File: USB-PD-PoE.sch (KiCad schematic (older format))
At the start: 126 parts, among them J1 8P8C_Shielded, J2 8P8C_Shielded, J3 TagConnect_TC2030_SWD, J4 USB_C_Receptacle_USB2.0, Q1 FDC2512, Q2 2N7002, Q3 2N7002, Q4 2N7002, Q5 APM4953KC, T1 HR051142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

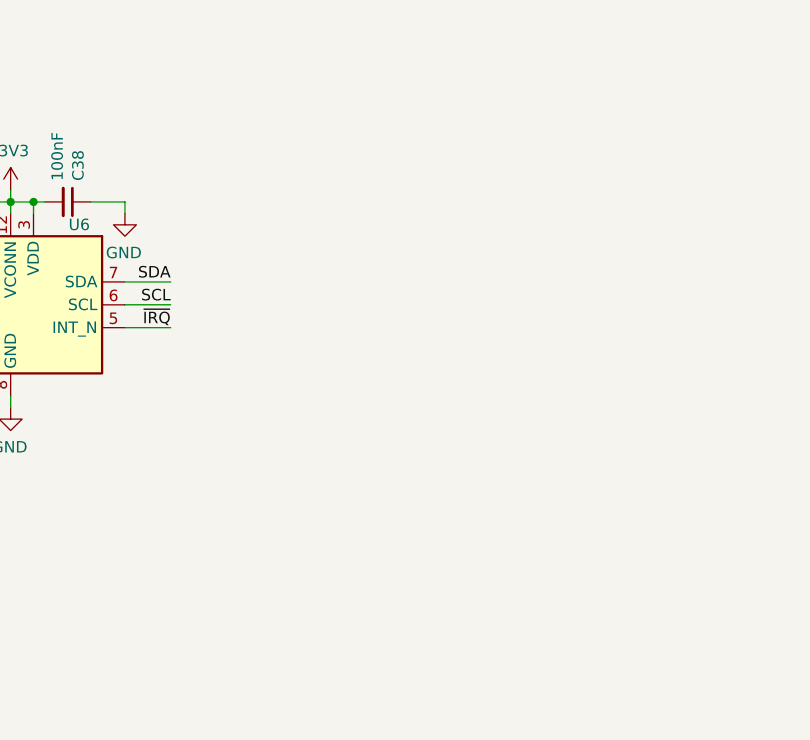
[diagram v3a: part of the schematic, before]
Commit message: Add USB/CC protection diode
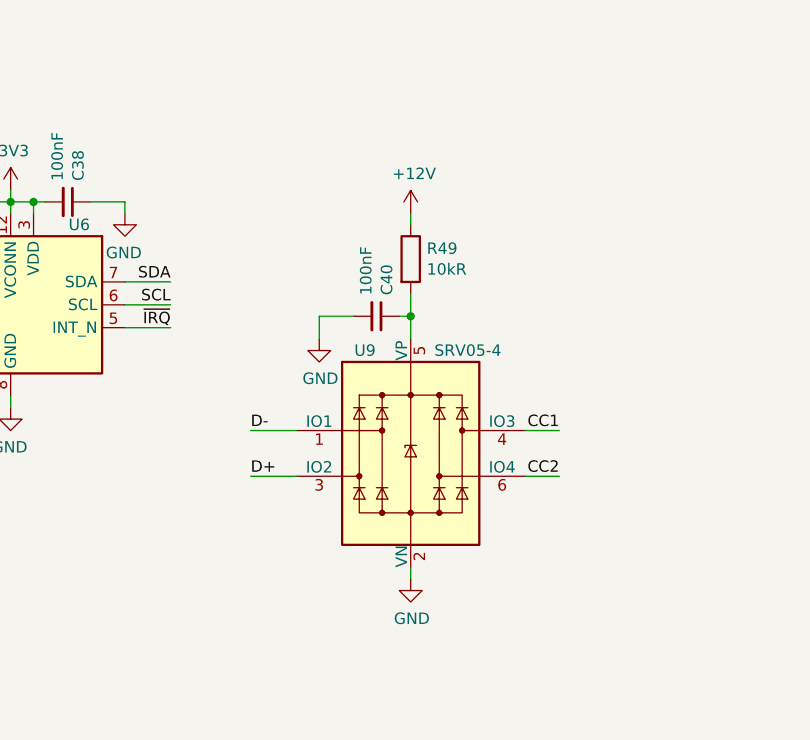
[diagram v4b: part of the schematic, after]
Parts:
- added C40: 100nF, Capacitor_SMD:C_0402_1005Metric, symbol Device:C_Small
- added R49: 10kR, Resistor_SMD:R_0402_1005Metric, symbol Device:R
- added U9: SRV05-4, Package_TO_SOT_SMD:SOT-23-6, symbol Power_Protection:SRV05-4
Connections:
- net +12V: now also R49.1
- net CC1: now also U9.4 (IO3)
- net CC2: now also U9.6 (IO4)
- net D+: now also U9.3 (IO2)
- net D-: now also U9.1 (IO1)
- net GND: now also C40.2, U9.2 (VN)
- new net: C40.1, R49.2, U9.5 (VP)
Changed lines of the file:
@@
 	1    0    0    -1
 $EndComp
+$Comp
+L Power_Protection:SRV05-4 U9
+U 1 1 64F616A2
+P 7800 9700
+F 0 "U9" H 7600 10150 50  0000 C CNN
+F 1 "SRV05-4" H 8050 10150 50  0000 C CNN
+F 2 "Package_TO_SOT_SMD:SOT-23-6" H 8500 9250 50  0001 C CNN
+F 3 "http://www.onsemi.com/pub/Collateral/SRV05-4-D.PDF" H 7800 9700 50  0001 C CNN
+F 4 "C85364" H 7800 9700 50  0001 C CNN "LCSC"
+	1    7800 9700
+	1    0    0    -1
+$EndComp
+$Comp
+L Device:R R49
+U 1 1 64F63DEA
+P 7800 8850
+F 0 "R49" H 7870 8896 50  0000 L CNN
+F 1 "10kR" H 7870 8805 50  0000 L CNN
+F 2 "Resistor_SMD:R_0402_1005Metric" V 7730 8850 50  0001 C CNN
+F 3 "~" H 7800 8850 50  0001 C CNN
+F 4 "C25744" H 7800 8850 50  0001 C CNN "LCSC"
+	1    7800 8850
+	1    0    0    -1
+$EndComp
+$Comp
+L Device:C_Small C40
+U 1 1 64FABF15
+P 7650 9100
+F 0 "C40" H 7742 9146 50  0000 L CNN
+F 1 "100nF" H 7742 9055 50  0000 L CNN
+F 2 "Capacitor_SMD:C_0402_1005Metric" H 7650 9100 50  0001 C CNN
+F 3 "~" H 7650 9100 50  0001 C CNN
+F 4 "C1525" H 7650 9100 50  0001 C CNN "LCSC"
+	1    7650 9100
+	0    1    -1   0
+$EndComp
+Wire Wire Line
+	7800 9200 7800 9100
+Wire Wire Line
+	7750 9100 7800 9100
+Connection ~ 7800 9100
+Wire Wire Line
+	7800 9100 7800 9000
+$Comp
+L power:GND #PWR0137
+U 1 1 65088998
+P 7400 9200
+F 0 "#PWR0137" H 7400 8950 50  0001 C CNN
+F 1 "GND" H 7405 9027 50  0000 C CNN
+F 2 "" H 7400 9200 50  0001 C CNN
+F 3 "" H 7400 9200 50  0001 C CNN
+	1    7400 9200
+	1    0    0    -1
+$EndComp
+Wire Wire Line
+	7400 9200 7400 9100
+Wire Wire Line
+	7400 9100 7550 9100
+$Comp
+L power:+12V #PWR0138
+U 1 1 650D4163
+P 7800 8650
+F 0 "#PWR0138" H 7800 8500 50  0001 C CNN
+F 1 "+12V" H 7815 8823 50  0000 C CNN
+F 2 "" H 7800 8650 50  0001 C CNN
+F 3 "" H 7800 8650 50  0001 C CNN
+	1    7800 8650
+	1    0    0    -1
+$EndComp
+Wire Wire Line
+	7800 8650 7800 8700
+Wire Wire Line
+	7300 9600 7100 9600
+Text Label 7100 9600 0    50   ~ 0
+D-
+Wire Wire Line
+	7300 9800 7100 9800
+Text Label 7100 9800 0    50   ~ 0
+D+
+Wire Wire Line
+	8300 9600 8450 9600
+Text Label 8450 9600 2    50   ~ 0
+CC1
+Wire Wire Line
+	8300 9800 8450 9800
+Text Label 8450 9800 2    50   ~ 0
+CC2
+$Comp
+L power:GND #PWR0139
+U 1 1 652C53BE
+P 7800 10250
+F 0 "#PWR0139" H 7800 10000 50  0001 C CNN
+F 1 "GND" H 7805 10077 50  0000 C CNN
+F 2 "" H 7800 10250 50  0001 C CNN
+F 3 "" H 7800 10250 50  0001 C CNN
+	1    7800 10250
+	1    0    0    -1
+$EndComp
+Wire Wire Line
+	7800 10250 7800 10200
 $EndSCHEMATC

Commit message: Fix reversed CJ431 pinout
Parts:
- U4: symbol Reference_Voltage:TL431DBZ -> Reference_Voltage:CJ432
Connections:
- net at C12.2, D7.2 (A), R17.2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: now also U4.2 (K); no longer U4.1 (K)
- net at C12.1, C13.1, R18.1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: now also U4.1 (REF); no longer U4.2 (REF)
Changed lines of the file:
@@
 	3350 1750 3350 2000
 $Comp
-L Reference_Voltage:TL431DBZ U4
+L Reference_Voltage:CJ432 U4
 U 1 1 60798E19
 P 6850 2400

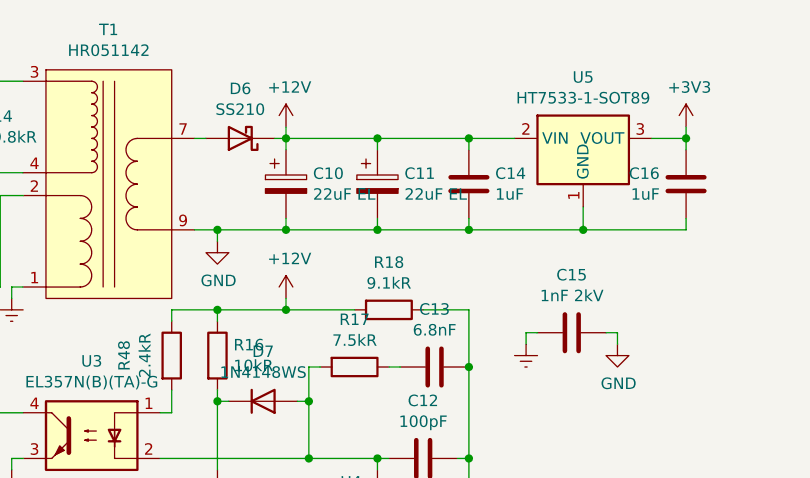
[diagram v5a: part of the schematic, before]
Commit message: Add more bulk capacitance on flyback output
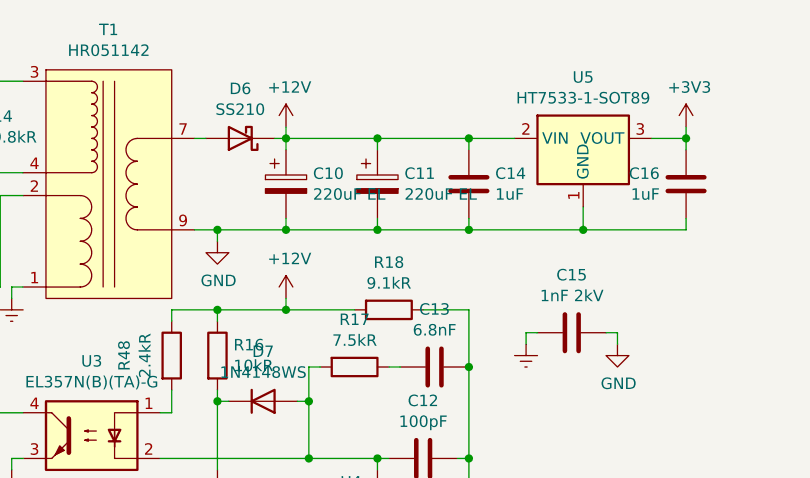
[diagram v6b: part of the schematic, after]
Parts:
- C10, C11: value 22uF EL -> 220uF EL; LCSC C134761 -> C127327
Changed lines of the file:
@@
 P 6450 1050
 F 0 "C10" H 6568 1096 50  0000 L CNN
-F 1 "22uF EL" H 6568 1005 50  0000 L CNN
+F 1 "220uF EL" H 6568 1005 50  0000 L CNN
 F 2 "Capacitor_SMD:CP_Elec_6.3x7.7" H 6488 900 50  0001 C CNN
 F 3 "~" H 6450 1050 50  0001 C CNN
-F 4 "C134761" H 6450 1050 50  0001 C CNN "LCSC"
+F 4 "C127327" H 6450 1050 50  0001 C CNN "LCSC"
 	1    6450 1050
 	1    0    0    -1
@@
 P 6850 1050
 F 0 "C11" H 6968 1096 50  0000 L CNN
-F 1 "22uF EL" H 6968 1005 50  0000 L CNN
+F 1 "220uF EL" H 6968 1005 50  0000 L CNN
 F 2 "Capacitor_SMD:CP_Elec_6.3x7.7" H 6888 900 50  0001 C CNN
 F 3 "~" H 6850 1050 50  0001 C CNN
-F 4 "C134761" H 6850 1050 50  0001 C CNN "LCSC"
+F 4 "C127327" H 6850 1050 50  0001 C CNN "LCSC"
 	1    6850 1050
 	1    0    0    -1

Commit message: Add buck converter power gating
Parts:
- added Q6: 2N7002, Package_TO_SOT_SMD:SOT-23, symbol Transistor_FET:2N7002
- added R50, R51: 100kR, Resistor_SMD:R_0402_1005Metric, symbol Device:R_Small
- added R52: 15kR, Resistor_SMD:R_0402_1005Metric, symbol Device:R_Small
- added R53: 10kR, Resistor_SMD:R_0402_1005Metric, symbol Device:R
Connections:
- net BOOST_OUT: no longer Q5.1 (S)
- net GND: now also Q6.2 (S), R50.1
- net VBUS: now also Q5.1 (S), R51.1; no longer C29.1, C31.1, C39.1, L3.2, Q5.7 (D), Q5.8 (G), R31.1
- net BUCK_OUT_EN: now reaches U1.25 (PC5)
- net BUCK_OUT_EN: now also Q6.1 (G), R50.2
- net at Q5.4 (G), R39.1: now also R53.1; no longer Q4.3 (D), Q5.2 (G)
- new net: Q5.2 (G), R51.2, R52.2
- new net: Q6.3 (D), R52.1
- new net: Q4.3 (D), R53.2
- new net BUCK_OUT: C29.1, C31.1, C39.1, L3.2, Q5.7 (D), Q5.8 (G), R31.1
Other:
- moved on the sheet: Q4, Q5A, R40
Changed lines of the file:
@@
 L Device:Q_DUAL_PMOS_S1G1S2G2D2D2D1D1 Q5
 U 1 1 62480DAF
-P 16950 2650
-F 0 "Q5" V 17375 2650 50  0000 C CNN
-F 1 "APM4953KC" V 17284 2650 50  0000 C CNN
-F 2 "Package_SO:SO-8_3.9x4.9mm_P1.27mm" H 17000 2650 50  0001 C CNN
-F 3 "~" H 17000 2650 50  0001 C CNN
-F 4 "C20897" H 16950 2650 50  0001 C CNN "LCSC"
-	1    16950 2650
-	0    1    -1   0
+P 17350 4700
+F 0 "Q5" V 17775 4700 50  0000 C CNN
+F 1 "APM4953KC" V 17684 4700 50  0000 C CNN
+F 2 "Package_SO:SO-8_3.9x4.9mm_P1.27mm" H 17400 4700 50  0001 C CNN
+F 3 "~" H 17400 4700 50  0001 C CNN
+F 4 "C20897" H 17350 4700 50  0001 C CNN "LCSC"
+	1    17350 4700
+	0    -1   -1   0
 $EndComp
 $Comp
@@
 Wire Wire Line
 	16750 2550 16650 2550
-Connection ~ 16750 2550
 $Comp
 L Device:R_Small R39
@@
 Wire Wire Line
 	16950 2900 16950 2850
-Connection ~ 16950 2850
 Wire Wire Line
 	16650 2900 16650 2550
 Connection ~ 16650 2550
-Wire Wire Line
-	16950 3050 16950 2900
-Connection ~ 16950 2900
-Text Label 16100 3250 0    50   ~ 0
+Text Label 16100 3500 0    50   ~ 0
 BOOST_OUT_EN
 Wire Wire Line
-	16100 3250 16600 3250
+	16100 3500 16600 3500
 $Comp
 L Transistor_FET:2N7002 Q2
@@
 L Transistor_FET:2N7002 Q4
 U 1 1 62639897
-P 16850 3250
-F 0 "Q4" H 17054 3296 50  0000 L CNN
-F 1 "2N7002" H 17054 3205 50  0000 L CNN
-F 2 "Package_TO_SOT_SMD:SOT-23" H 17050 3175 50  0001 L CIN
-F 3 "https://www.onsemi.com/pub/Collateral/NDS7002A-D.PDF" H 16850 3250 50  0001 L CNN
-F 4 "C8545" H 16850 3250 50  0001 C CNN "LCSC"
-	1    16850 3250
+P 16850 3500
+F 0 "Q4" H 17054 3546 50  0000 L CNN
+F 1 "2N7002" H 17054 3455 50  0000 L CNN
+F 2 "Package_TO_SOT_SMD:SOT-23" H 17050 3425 50  0001 L CIN
+F 3 "https://www.onsemi.com/pub/Collateral/NDS7002A-D.PDF" H 16850 3500 50  0001 L CNN
+F 4 "C8545" H 16850 3500 50  0001 C CNN "LCSC"
+	1    16850 3500
 	1    0    0    -1
 $EndComp
@@
 L Device:R_Small R40
 U 1 1 62666D7F
-P 16800 3500
-F 0 "R40" H 16859 3546 50  0000 L CNN
-F 1 "100kR" H 16859 3455 50  0000 L CNN
-F 2 "Resistor_SMD:R_0402_1005Metric" H 16800 3500 50  0001 C CNN
-F 3 "~" H 16800 3500 50  0001 C CNN
-F 4 "C25741" H 16800 3500 50  0001 C CNN "LCSC"
-	1    16800 3500
+P 16800 3750
+F 0 "R40" H 16859 3796 50  0000 L CNN
+F 1 "100kR" H 16859 3705 50  0000 L CNN
+F 2 "Resistor_SMD:R_0402_1005Metric" H 16800 3750 50  0001 C CNN
+F 3 "~" H 16800 3750 50  0001 C CNN
+F 4 "C25741" H 16800 3750 50  0001 C CNN "LCSC"
+	1    16800 3750
 	0    1    1    0
 $EndComp
 Wire Wire Line
-	16900 3500 16950 3500
-Wire Wire Line
-	16950 3500 16950 3450
-Wire Wire Line
-	16700 3500 16600 3500
-Wire Wire Line
-	16600 3500 16600 3250
-Connection ~ 16600 3250
-Wire Wire Line
-	16600 3250 16650 3250
+	16900 3750 16950 3750
+Wire Wire Line
+	16950 3750 16950 3700
+Wire Wire Line
+	16700 3750 16600 3750
+Wire Wire Line
+	16600 3750 16600 3500
+Connection ~ 16600 3500
+Wire Wire Line
+	16600 3500 16650 3500
 $Comp
 L power:GND #PWR0118
 U 1 1 626E8989
-P 16950 3550
-F 0 "#PWR0118" H 16950 3300 50  0001 C CNN
-F 1 "GND" H 16955 3377 50  0000 C CNN
-F 2 "" H 16950 3550 50  0001 C CNN
-F 3 "" H 16950 3550 50  0001 C CNN
-	1    16950 3550
-	1    0    0    -1
-$EndComp
-Wire Wire Line
-	16950 3550 16950 3500
-Connection ~ 16950 3500
+P 16950 3800
+F 0 "#PWR0118" H 16950 3550 50  0001 C CNN
+F 1 "GND" H 16955 3627 50  0000 C CNN
+F 2 "" H 16950 3800 50  0001 C CNN
+F 3 "" H 16950 3800 50  0001 C CNN
+	1    16950 3800
+	1    0    0    -1
+$EndComp
+Wire Wire Line
+	16950 3800 16950 3750
+Connection ~ 16950 3750
 $Comp
 L power:VBUS #PWR0119
@@
 Wire Wire Line
 	17150 2450 17200 2450
-Connection ~ 17150 2450
 Wire Wire Line
 	17150 2550 17200 2550
 Wire Wire Line
 	17200 2550 17200 2450
-Connection ~ 17150 2550
 Connection ~ 17200 2450
 Wire Wire Line
@@
 Wire Wire Line
 	16400 4650 16400 4600
-Connection ~ 16400 4600
-Wire Wire Line
-	16400 4600 17750 4600
 Wire Wire Line
 	16400 4850 16400 4900
@@
 Wire Wire Line
 	7800 10250 7800 10200
+Wire Wire Line
+	17550 4600 17650 4600
+Wire Wire Line
+	17150 4600 17100 4600
+Connection ~ 16400 4600
+Wire Wire Line
+	17150 4500 17100 4500
+Wire Wire Line
+	17100 4500 17100 4600
+Connection ~ 17100 4600
+Wire Wire Line
+	17100 4600 16400 4600
+$Comp
+L Device:R_Small R51
+U 1 1 60885FEE
+P 17500 4950
+F 0 "R51" H 17559 4996 50  0000 L CNN
+F 1 "100kR" H 17559 4905 50  0000 L CNN
+F 2 "Resistor_SMD:R_0402_1005Metric" H 17500 4950 50  0001 C CNN
+F 3 "~" H 17500 4950 50  0001 C CNN
+F 4 "C25741" H 17500 4950 50  0001 C CNN "LCSC"
+	1    17500 4950
+	0    1    1    0
+$EndComp
+Wire Wire Line
+	17350 4900 17350 4950
+Wire Wire Line
+	17350 4950 17400 4950
+Wire Wire Line
+	17650 4600 17650 4950
+Wire Wire Line
+	17650 4950 17600 4950
+Connection ~ 17650 4600
+Wire Wire Line
+	17650 4600 17750 4600
+Wire Wire Line
+	17050 5600 17050 5800
+Wire Wire Line
+	17250 5800 17350 5800
+Text Label 16500 5600 0    50   ~ 0
+BUCK_OUT_EN
+$Comp
+L power:GND #PWR0140
+U 1 1 6097046C
+P 17350 5850
+F 0 "#PWR0140" H 17350 5600 50  0001 C CNN
+F 1 "GND" H 17355 5677 50  0000 C CNN
+F 2 "" H 17350 5850 50  0001 C CNN
+F 3 "" H 17350 5850 50  0001 C CNN
+	1    17350 5850
+	1    0    0    -1
+$EndComp
+Wire Wire Line
+	17350 5850 17350 5800
+$Comp
+L Device:R_Small R50
+U 1 1 60970474
+P 17150 5800
+F 0 "R50" H 17209 5846 50  0000 L CNN
+F 1 "100kR" H 17209 5755 50  0000 L CNN
+F 2 "Resistor_SMD:R_0402_1005Metric" H 17150 5800 50  0001 C CNN
+F 3 "~" H 17150 5800 50  0001 C CNN
+F 4 "C25741" H 17150 5800 50  0001 C CNN "LCSC"
+	1    17150 5800
+	0    1    1    0
+$EndComp
+$Comp
+L Transistor_FET:2N7002 Q6
+U 1 1 6097047B
+P 17250 5600
+F 0 "Q6" H 17454 5646 50  0000 L CNN
+F 1 "2N7002" H 17454 5555 50  0000 L CNN
+F 2 "Package_TO_SOT_SMD:SOT-23" H 17450 5525 50  0001 L CIN
+F 3 "https://www.onsemi.com/pub/Collateral/NDS7002A-D.PDF" H 17250 5600 50  0001 L CNN
+F 4 "C8545" H 17250 5600 50  0001 C CNN "LCSC"
+	1    17250 5600
+	1    0    0    -1
+$EndComp
+Connection ~ 17350 5800
+Connection ~ 17050 5600
+Wire Wire Line
+	16500 5600 17050 5600
+Text Label -4950 5350 0    50   ~ 0
+BUCK_OUT_EN
+Wire Wire Line
+	-4950 5350 -4400 5350
+$Comp
+L Device:R_Small R52
+U 1 1 60B3D914
+P 17350 5250
+F 0 "R52" H 17409 5296 50  0000 L CNN
+F 1 "15kR" H 17409 5205 50  0000 L CNN
+F 2 "Resistor_SMD:R_0402_1005Metric" H 17350 5250 50  0001 C CNN
+F 3 "~" H 17350 5250 50  0001 C CNN
+F 4 "C25756" H 17350 5250 50  0001 C CNN "LCSC"
+	1    17350 5250
+	-1   0    0    1
+$EndComp
+Wire Wire Line
+	17350 5400 17350 5350
+Wire Wire Line
+	17350 5150 17350 4950
+Connection ~ 17350 4950
+$Comp
+L Device:R R53
+U 1 1 60C301E8
+P 16950 3100
+F 0 "R53" H 17020 3146 50  0000 L CNN
+F 1 "10kR" H 17020 3055 50  0000 L CNN
+F 2 "Resistor_SMD:R_0402_1005Metric" V 16880 3100 50  0001 C CNN
+F 3 "~" H 16950 3100 50  0001 C CNN
+F 4 "C25744" H 16950 3100 50  0001 C CNN "LCSC"
+	1    16950 3100
+	1    0    0    -1
+$EndComp
+Wire Wire Line
+	16950 2950 16950 2900
+Connection ~ 16950 2900
+Wire Wire Line
+	16950 3250 16950 3300
 $EndSCHEMATC

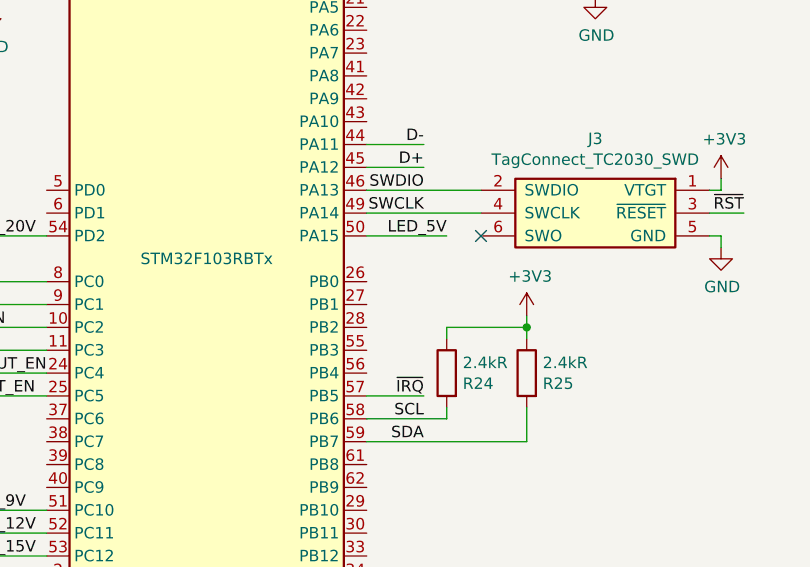
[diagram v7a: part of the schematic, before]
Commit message: Move 5V LED away from JTAG pins
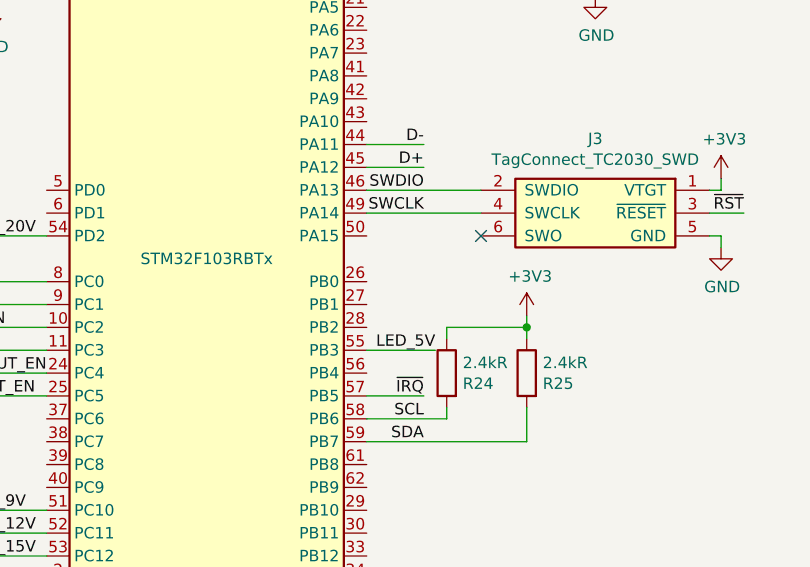
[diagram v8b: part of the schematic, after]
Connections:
- net LED_5V: now also U1.55 (PB3); no longer U1.50 (PA15)
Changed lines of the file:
@@
 Wire Wire Line
 	-6150 7150 -6150 7100
-Text Label -2650 4650 2    50   ~ 0
+Text Label -2700 5150 2    50   ~ 0
 LED_5V
-Wire Wire Line
-	-3000 4650 -2650 4650
 Text Label -4750 5850 0    50   ~ 0
 LED_9V
@@
 Wire Wire Line
 	16950 3250 16950 3300
+Wire Wire Line
+	-2700 5150 -3000 5150
 $EndSCHEMATC
